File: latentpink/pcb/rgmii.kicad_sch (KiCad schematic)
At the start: 58 parts, among them J5 0826-1G1T-23-F, U2 XC7K160T-2FBG484C, U21 ECX2-LMV-3CN-125.000-TR, U22 ECS-2016MVQ-250-CN, U9 KSZ9031RN

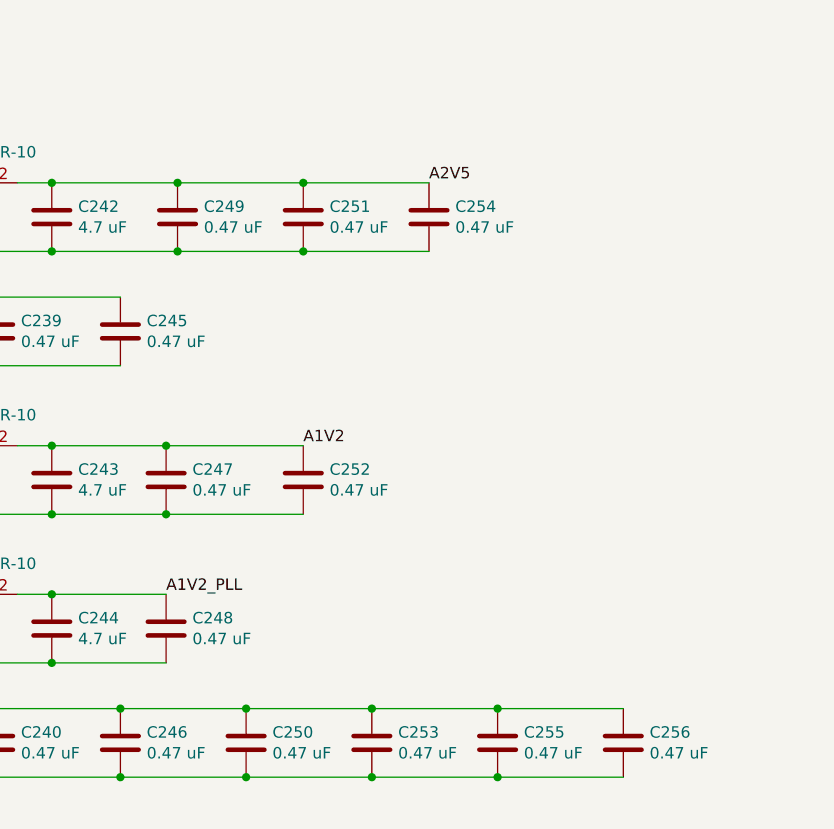
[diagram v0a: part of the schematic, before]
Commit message: Continued work on signoff review, added some more test points and SFP+ activity LEDs
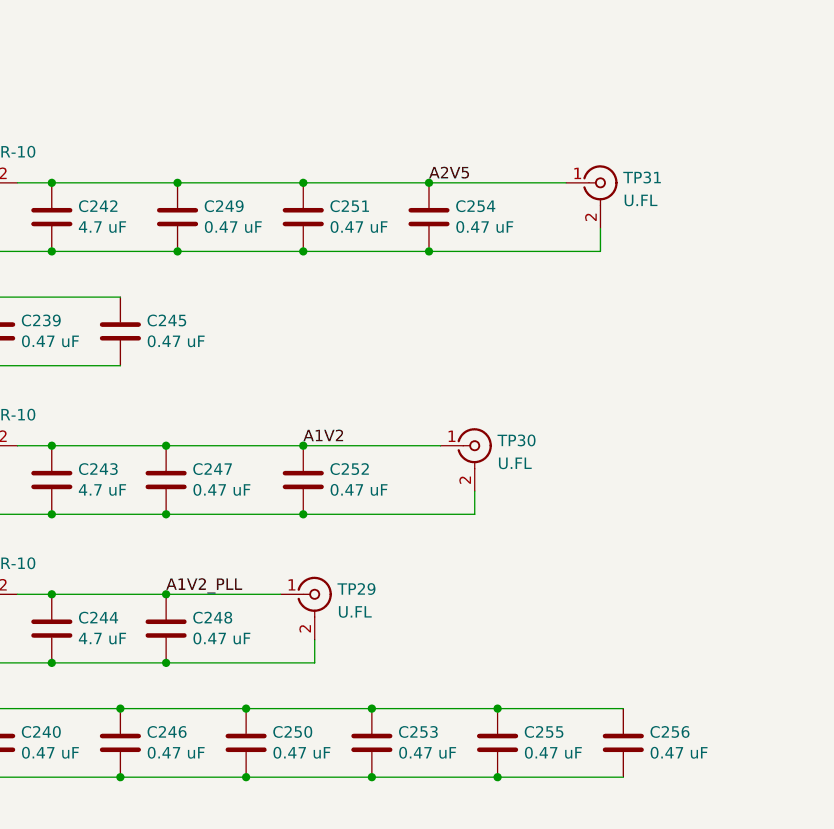
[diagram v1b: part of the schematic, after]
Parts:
- added TP29, TP30, TP31: U.FL, azonenberg_pcb:CONN_U.FL_TE_1909763-1, symbol conn:CONN_COAXIAL
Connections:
- net A1V2: now also TP30.1 (In)
- net A1V2_PLL: now also TP29.1 (In)
- net A2V5: now also TP31.1 (In)
- net GND: now also TP29.2 (Ext), TP30.2 (Ext), TP31.2 (Ext)
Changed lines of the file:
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@@
   (paper "A3")
   (title_block
-    (date "2023-05-20")
+    (date "2023-05-21")
   )
   (junction (at 95.25 53.34) (diameter 0) (color 0 0 0 0)
@@
   (junction (at 96.52 135.89) (diameter 0) (color 0 0 0 0)
   )
+  (junction (at 96.52 165.1) (diameter 0) (color 0 0 0 0)
+  )
   (junction (at 62.23 201.93) (diameter 0) (color 0 0 0 0)
   )
@@
   (junction (at 95.25 35.56) (diameter 0) (color 0 0 0 0)
   )
+  (junction (at 96.52 172.72) (diameter 0) (color 0 0 0 0)
+  )
   (junction (at 68.58 172.72) (diameter 0) (color 0 0 0 0)
   )
@@
   (junction (at 90.17 201.93) (diameter 0) (color 0 0 0 0)
   )
+  (junction (at 110.49 135.89) (diameter 0) (color 0 0 0 0)
+  )
   (junction (at 62.23 148.59) (diameter 0) (color 0 0 0 0)
   )
+  (junction (at 81.28 189.23) (diameter 0) (color 0 0 0 0)
+  )
+  (junction (at 81.28 181.61) (diameter 0) (color 0 0 0 0)
+  )
   (junction (at 62.23 194.31) (diameter 0) (color 0 0 0 0)
   )
@@
   )
   (junction (at 82.55 135.89) (diameter 0) (color 0 0 0 0)
+  )
+  (junction (at 110.49 143.51) (diameter 0) (color 0 0 0 0)
   )
   (junction (at 81.28 165.1) (diameter 0) (color 0 0 0 0)
@@
     (stroke (width 0) (type default) (color 0 0 0 0))
   )
+  (wire (pts (xy 110.49 143.51) (xy 129.54 143.51))
+    (stroke (width 0) (type default) (color 0 0 0 0))
+  )
   (wire (pts (xy 43.18 46.99) (xy 46.99 46.99))
     (stroke (width 0) (type default) (color 0 0 0 0))
@@
     (stroke (width 0) (type default) (color 0 0 0 0))
   )
+  (wire (pts (xy 81.28 189.23) (xy 97.79 189.23))
+    (stroke (width 0) (type default) (color 0 0 0 0))
+  )
   (wire (pts (xy 170.18 67.31) (xy 163.83 67.31))
     (stroke (width 0) (type default) (color 0 0 0 0))
@@
     (stroke (width 0) (type default) (color 0 0 0 0))
   )
+  (wire (pts (xy 129.54 143.51) (xy 129.54 140.97))
+    (stroke (width 0) (type default) (color 0 0 0 0))
+  )
   (wire (pts (xy 219.71 67.31) (xy 214.63 67.31))
     (stroke (width 0) (type default) (color 0 0 0 0))
@@
     (stroke (width 0) (type default) (color 0 0 0 0))
   )
+  (wire (pts (xy 115.57 172.72) (xy 115.57 170.18))
+    (stroke (width 0) (type default) (color 0 0 0 0))
+  )
   (wire (pts (xy 163.83 59.69) (xy 170.18 59.69))
     (stroke (width 0) (type default) (color 0 0 0 0))
@@
     (stroke (width 0) (type default) (color 0 0 0 0))
   )
+  (wire (pts (xy 97.79 189.23) (xy 97.79 186.69))
+    (stroke (width 0) (type default) (color 0 0 0 0))
+  )
   (wire (pts (xy 54.61 135.89) (xy 49.53 135.89))
     (stroke (width 0) (type default) (color 0 0 0 0))
@@
     (stroke (width 0) (type default) (color 0 0 0 0))
   )
+  (wire (pts (xy 96.52 172.72) (xy 115.57 172.72))
+    (stroke (width 0) (type default) (color 0 0 0 0))
+  )
   (wire (pts (xy 163.83 54.61) (xy 170.18 54.61))
     (stroke (width 0) (type default) (color 0 0 0 0))
@@
     (stroke (width 0) (type default) (color 0 0 0 0))
   )
+  (wire (pts (xy 110.49 135.89) (xy 125.73 135.89))
+    (stroke (width 0) (type default) (color 0 0 0 0))
+  )
+  (wire (pts (xy 81.28 181.61) (xy 93.98 181.61))
+    (stroke (width 0) (type default) (color 0 0 0 0))
+  )
   (wire (pts (xy 156.21 62.23) (xy 152.4 62.23))
     (stroke (width 0) (type default) (color 0 0 0 0))
@@
   )
   (wire (pts (xy 156.21 57.15) (xy 152.4 57.15))
+    (stroke (width 0) (type default) (color 0 0 0 0))
+  )
+  (wire (pts (xy 96.52 165.1) (xy 111.76 165.1))
     (stroke (width 0) (type default) (color 0 0 0 0))
   )
@@
     )
     (property "Datasheet" "" (id 3) (at 96.52 139.7 0)
+      (effects (font (size 1.27 1.27)) hide)
+    )
+    (pin "1")
+    (pin "2")
+  )
+  (symbol (lib_id "conn:CONN_COAXIAL") (at 129.54 135.89 0) (unit 1)
+    (in_bom yes) (on_board yes) (fields_autoplaced)
+    (property "Reference" "TP31" (id 0) (at 132.0801 135.3485 0)
+      (effects (font (size 1.27 1.27)) (justify left))
+    )
+    (property "Value" "U.FL" (id 1) (at 132.0801 137.8854 0)
+      (effects (font (size 1.27 1.27)) (justify left))
+    )
+    (property "Footprint" "azonenberg_pcb:CONN_U.FL_TE_1909763-1" (id 2) (at 129.54 135.89 0)
+      (effects (font (size 1.27 1.27)) hide)
+    )
+    (property "Datasheet" "" (id 3) (at 129.54 135.89 0)
       (effects (font (size 1.27 1.27)) hide)
     )
@@
     )
     (property "Datasheet" "" (id 3) (at 160.02 54.61 0)
+      (effects (font (size 1.27 1.27)) hide)
+    )
+    (pin "1")
+    (pin "2")
+  )
+  (symbol (lib_id "conn:CONN_COAXIAL") (at 115.57 165.1 0) (unit 1)
+    (in_bom yes) (on_board yes) (fields_autoplaced)
+    (property "Reference" "TP30" (id 0) (at 118.1101 164.5585 0)
+      (effects (font (size 1.27 1.27)) (justify left))
+    )
+    (property "Value" "U.FL" (id 1) (at 118.1101 167.0954 0)
+      (effects (font (size 1.27 1.27)) (justify left))
+    )
+    (property "Footprint" "azonenberg_pcb:CONN_U.FL_TE_1909763-1" (id 2) (at 115.57 165.1 0)
+      (effects (font (size 1.27 1.27)) hide)
+    )
+    (property "Datasheet" "" (id 3) (at 115.57 165.1 0)
       (effects (font (size 1.27 1.27)) hide)
     )
@@
       (effects (font (size 1.27 1.27)) hide)
     )
+    (pin "1")
+    (pin "2")
+  )
+  (symbol (lib_id "conn:CONN_COAXIAL") (at 97.79 181.61 0) (unit 1)
+    (in_bom yes) (on_board yes) (fields_autoplaced)
+    (property "Reference" "TP29" (id 0) (at 100.3301 181.0685 0)
+      (effects (font (size 1.27 1.27)) (justify left))
+    )
+    (property "Value" "U.FL" (id 1) (at 100.3301 183.6054 0)
+      (effects (font (size 1.27 1.27)) (justify left))
+    )
+    (property "Footprint" "azonenberg_pcb:CONN_U.FL_TE_1909763-1" (id 2) (at 97.79 181.61 0)
+      (effects (font (size 1.27 1.27)) hide)
+    )
+    (property "Datasheet" "" (id 3) (at 97.79 181.61 0)
+      (effects (font (size 1.27 1.27)) hide)
+    )

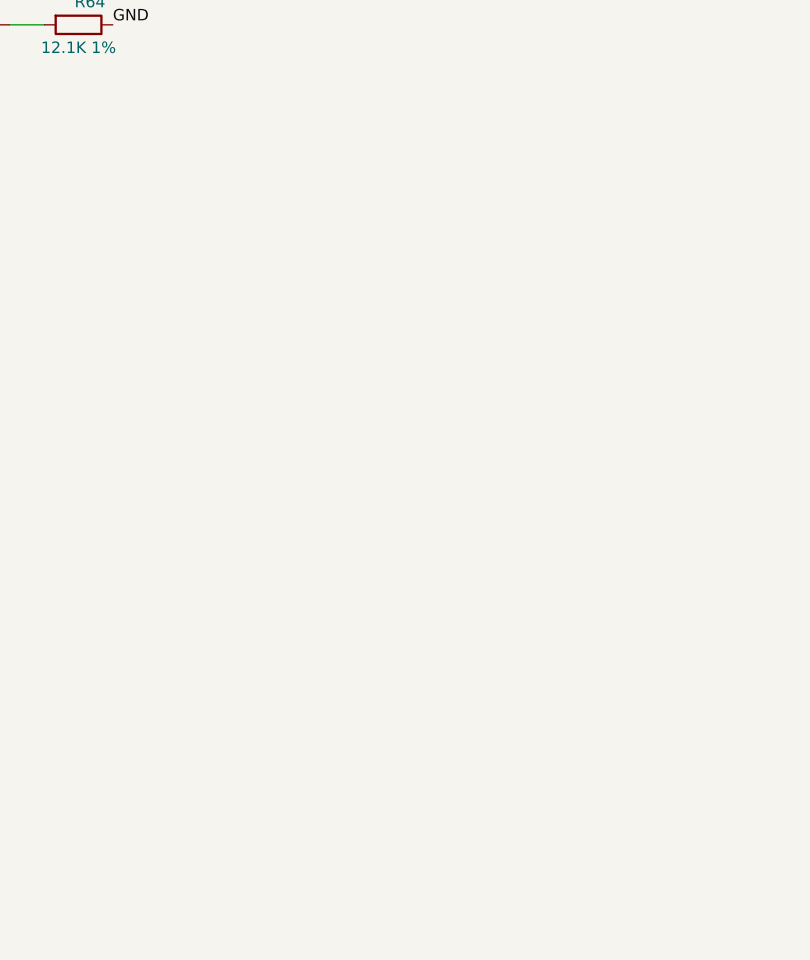
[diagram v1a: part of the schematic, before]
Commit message: Finished initial schematic review, added ESD diodes to Ethernet pairs
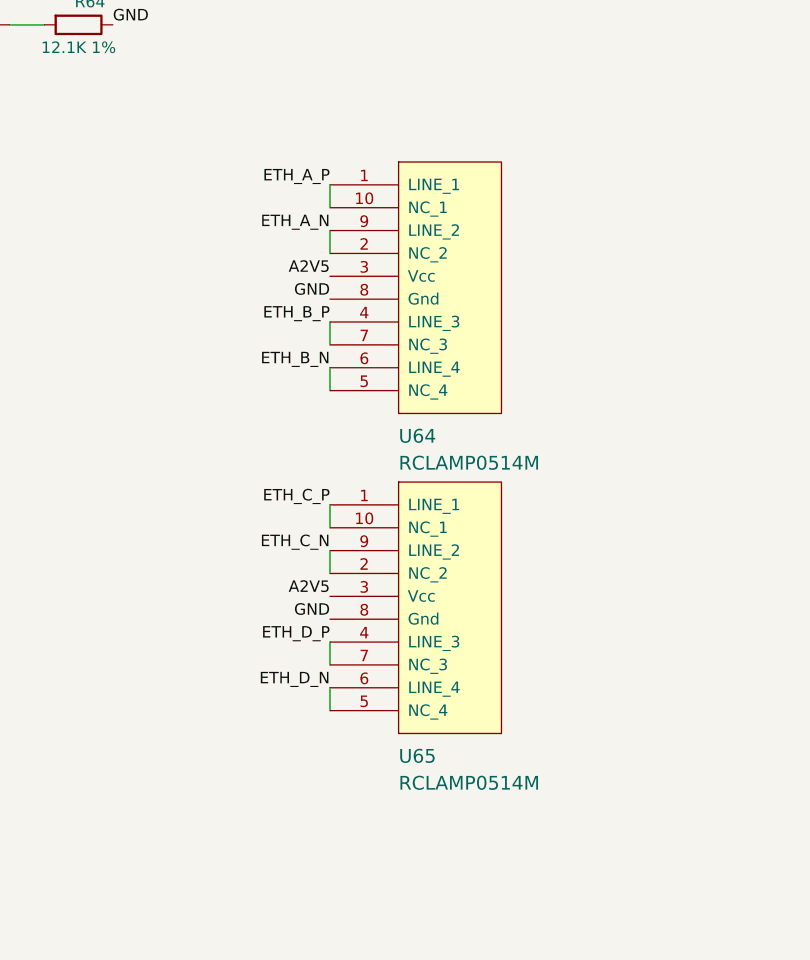
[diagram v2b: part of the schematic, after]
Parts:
- added U64, U65: RCLAMP0514M, azonenberg_pcb:SOP_10_0.5MM_3MM, symbol special-azonenberg:RCLAMP0514M
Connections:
- net A2V5: now also U64.3 (Vcc), U65.3 (Vcc)
- net ETH_A_N: now also U64.2 (NC_2), U64.9 (LINE_2)
- net ETH_A_P: now also U64.1 (LINE_1), U64.10 (NC_1)
- net ETH_B_N: now also U64.5 (NC_4), U64.6 (LINE_4)
- net ETH_B_P: now also U64.4 (LINE_3), U64.7 (NC_3)
- net ETH_C_N: now also U65.2 (NC_2), U65.9 (LINE_2)
- net ETH_C_P: now also U65.1 (LINE_1), U65.10 (NC_1)
- net ETH_D_N: now also U65.5 (NC_4), U65.6 (LINE_4)
- net ETH_D_P: now also U65.4 (LINE_3), U65.7 (NC_3)
- net GND: now also U64.8 (Gnd), U65.8 (Gnd)
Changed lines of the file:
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@@
+    (stroke (width 0) (type default) (color 0 0 0 0))
+  )
+  (wire (pts (xy 187.96 116.84) (xy 187.96 119.38))
     (stroke (width 0) (type default) (color 0 0 0 0))
   )
@@
     (stroke (width 0) (type default) (color 0 0 0 0))
   )
+  (wire (pts (xy 187.96 162.56) (xy 187.96 165.1))
+    (stroke (width 0) (type default) (color 0 0 0 0))
+  )
   (wire (pts (xy 68.58 172.72) (xy 81.28 172.72))
     (stroke (width 0) (type default) (color 0 0 0 0))
@@
     (stroke (width 0) (type default) (color 0 0 0 0))
   )
+  (wire (pts (xy 187.96 111.76) (xy 187.96 114.3))
+    (stroke (width 0) (type default) (color 0 0 0 0))
+  )
   (wire (pts (xy 95.25 72.39) (xy 95.25 74.93))
     (stroke (width 0) (type default) (color 0 0 0 0))
@@
     (stroke (width 0) (type default) (color 0 0 0 0))
   )
+  (wire (pts (xy 187.96 127) (xy 187.96 129.54))
+    (stroke (width 0) (type default) (color 0 0 0 0))
+  )
+  (wire (pts (xy 187.96 132.08) (xy 187.96 134.62))
+    (stroke (width 0) (type default) (color 0 0 0 0))
+  )
   (wire (pts (xy 166.37 77.47) (xy 152.4 77.47))
     (stroke (width 0) (type default) (color 0 0 0 0))
@@
     (stroke (width 0) (type default) (color 0 0 0 0))
   )
+  (wire (pts (xy 187.96 167.64) (xy 187.96 170.18))
+    (stroke (width 0) (type default) (color 0 0 0 0))
+  )
   (wire (pts (xy 96.52 172.72) (xy 115.57 172.72))
     (stroke (width 0) (type default) (color 0 0 0 0))
@@
     (stroke (width 0) (type default) (color 0 0 0 0))
   )
+  (wire (pts (xy 187.96 147.32) (xy 187.96 149.86))
+    (stroke (width 0) (type default) (color 0 0 0 0))
+  )
   (wire (pts (xy 49.53 172.72) (xy 68.58 172.72))
     (stroke (width 0) (type default) (color 0 0 0 0))
@@
   )
   (wire (pts (xy 168.91 25.4) (xy 168.91 30.48))
+    (stroke (width 0) (type default) (color 0 0 0 0))
+  )
+  (wire (pts (xy 187.96 152.4) (xy 187.96 154.94))
     (stroke (width 0) (type default) (color 0 0 0 0))
   )
@@
     (effects (font (size 1.27 1.27)) (justify right bottom))
   )
+  (label "GND" (at 187.96 160.02 180)
+    (effects (font (size 1.27 1.27)) (justify right bottom))
+  )
   (label "ETH_RXD3" (at 293.37 85.09 180)
     (effects (font (size 1.27 1.27)) (justify right bottom))
@@
     (effects (font (size 1.27 1.27)) (justify right bottom))
   )
+  (label "ETH_D_P" (at 187.96 162.56 180)
+    (effects (font (size 1.27 1.27)) (justify right bottom))
+  )
   (label "ETH_LED1_N_1V8" (at 293.37 158.75 180)
     (effects (font (size 1.27 1.27)) (justify right bottom))
@@
     (effects (font (size 1.27 1.27)) (justify right bottom))
   )
+  (label "ETH_B_P" (at 187.96 127 180)
+    (effects (font (size 1.27 1.27)) (justify right bottom))
+  )
   (label "ETH_B_P" (at 43.18 69.85 0)
     (effects (font (size 1.27 1.27)) (justify left bottom))
@@
     (effects (font (size 1.27 1.27)) (justify left bottom))
   )
+  (label "GND" (at 187.96 124.46 180)
+    (effects (font (size 1.27 1.27)) (justify right bottom))
+  )
+  (label "ETH_B_N" (at 187.96 132.08 180)
+    (effects (font (size 1.27 1.27)) (justify right bottom))
+  )
   (label "1V8" (at 173.99 77.47 0)
     (effects (font (size 1.27 1.27)) (justify left bottom))
@@
     (effects (font (size 1.27 1.27)) (justify left bottom))
   )
+  (label "ETH_D_N" (at 187.96 167.64 180)
+    (effects (font (size 1.27 1.27)) (justify right bottom))
+  )
   (label "GND" (at 58.42 92.71 0)
     (effects (font (size 1.27 1.27)) (justify left bottom))
@@
     (effects (font (size 1.27 1.27)) (justify left bottom))
   )
+  (label "ETH_C_N" (at 187.96 152.4 180)
+    (effects (font (size 1.27 1.27)) (justify right bottom))
+  )
   (label "ETH_C_P" (at 43.18 80.01 0)
     (effects (font (size 1.27 1.27)) (justify left bottom))
@@
     (effects (font (size 1.27 1.27)) (justify right bottom))
   )
+  (label "ETH_A_N" (at 187.96 116.84 180)
+    (effects (font (size 1.27 1.27)) (justify right bottom))
+  )
   (label "1V8" (at 218.44 80.01 0)
     (effects (font (size 1.27 1.27)) (justify left bottom))
@@
     (effects (font (size 1.27 1.27)) (justify right bottom))
   )
+  (label "ETH_A_P" (at 187.96 111.76 180)
+    (effects (font (size 1.27 1.27)) (justify right bottom))
+  )
   (label "1V2" (at 49.53 181.61 180)
     (effects (font (size 1.27 1.27)) (justify right bottom))
   )
+  (label "ETH_C_P" (at 187.96 147.32 180)
+    (effects (font (size 1.27 1.27)) (justify right bottom))
+  )
   (label "GND" (at 43.18 54.61 0)
     (effects (font (size 1.27 1.27)) (justify left bottom))
@@
     (effects (font (size 1.27 1.27)) (justify left bottom))
   )
+  (label "A2V5" (at 187.96 157.48 180)
+    (effects (font (size 1.27 1.27)) (justify right bottom))
+  )
   (label "ETH_B_N" (at 43.18 74.93 0)
     (effects (font (size 1.27 1.27)) (justify left bottom))
@@
   (label "ETH_RXD3" (at 170.18 54.61 0)
     (effects (font (size 1.27 1.27)) (justify left bottom))
+  )
+  (label "A2V5" (at 187.96 121.92 180)
+    (effects (font (size 1.27 1.27)) (justify right bottom))
   )
   (hierarchical_label "2V5" (shape input) (at 49.53 135.89 180)
@@
     (pin "2")
   )
+  (symbol (lib_id "special-azonenberg:RCLAMP0514M") (at 195.58 172.72 0) (unit 1)
+    (in_bom yes) (on_board yes)
+    (property "Reference" "U65" (id 0) (at 195.58 175.26 0)
+      (effects (font (size 1.524 1.524)) (justify left))
+    )
+    (property "Value" "RCLAMP0514M" (id 1) (at 195.58 178.2534 0)
+      (effects (font (size 1.524 1.524)) (justify left))
+    )
+    (property "Footprint" "azonenberg_pcb:SOP_10_0.5MM_3MM" (id 2) (at 195.58 172.72 0)
+      (effects (font (size 1.524 1.524)) hide)
+    )
+    (property "Datasheet" "" (id 3) (at 195.58 172.72 0)
+      (effects (font (size 1.524 1.524)))
+    )
+    (pin "1")
+    (pin "10")
+    (pin "2")
+    (pin "3")
+    (pin "4")
+    (pin "5")
+    (pin "6")
+    (pin "7")
+    (pin "8")
+    (pin "9")
+  )
   (symbol (lib_id "device:C") (at 62.23 152.4 0) (unit 1)
     (in_bom yes) (on_board yes)
@@
     (pin "2")
   )
+  (symbol (lib_id "special-azonenberg:RCLAMP0514M") (at 195.58 137.16 0) (unit 1)
+    (in_bom yes) (on_board yes)
+    (property "Reference" "U64" (id 0) (at 195.58 139.7 0)
+      (effects (font (size 1.524 1.524)) (justify left))
+    )
+    (property "Value" "RCLAMP0514M" (id 1) (at 195.58 142.6934 0)
+      (effects (font (size 1.524 1.524)) (justify left))
+    )
+    (property "Footprint" "azonenberg_pcb:SOP_10_0.5MM_3MM" (id 2) (at 195.58 137.16 0)
+      (effects (font (size 1.524 1.524)) hide)
+    )
+    (property "Datasheet" "" (id 3) (at 195.58 137.16 0)
+      (effects (font (size 1.524 1.524)))
+    )
+    (pin "1")
+    (pin "10")
+    (pin "2")
+    (pin "3")
+    (pin "4")
+    (pin "5")
+    (pin "6")
+    (pin "7")
+    (pin "8")
+    (pin "9")
+  )
   (symbol (lib_id "device:R") (at 50.8 46.99 270) (unit 1)
